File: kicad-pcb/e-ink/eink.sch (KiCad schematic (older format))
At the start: 80 parts, among them J2 Conn_01x39_Female, J3 Conn_01x08_Female, Q1 IRLML6402, U1 TS512BIYDT, U2 LT1945, U3 LM79L15ACM_NOPB, U4 LM78L15ACM_NOPB, U5 TPS62177DQC, U6 MCP23S17_SO, U8 MCP23S17_SO

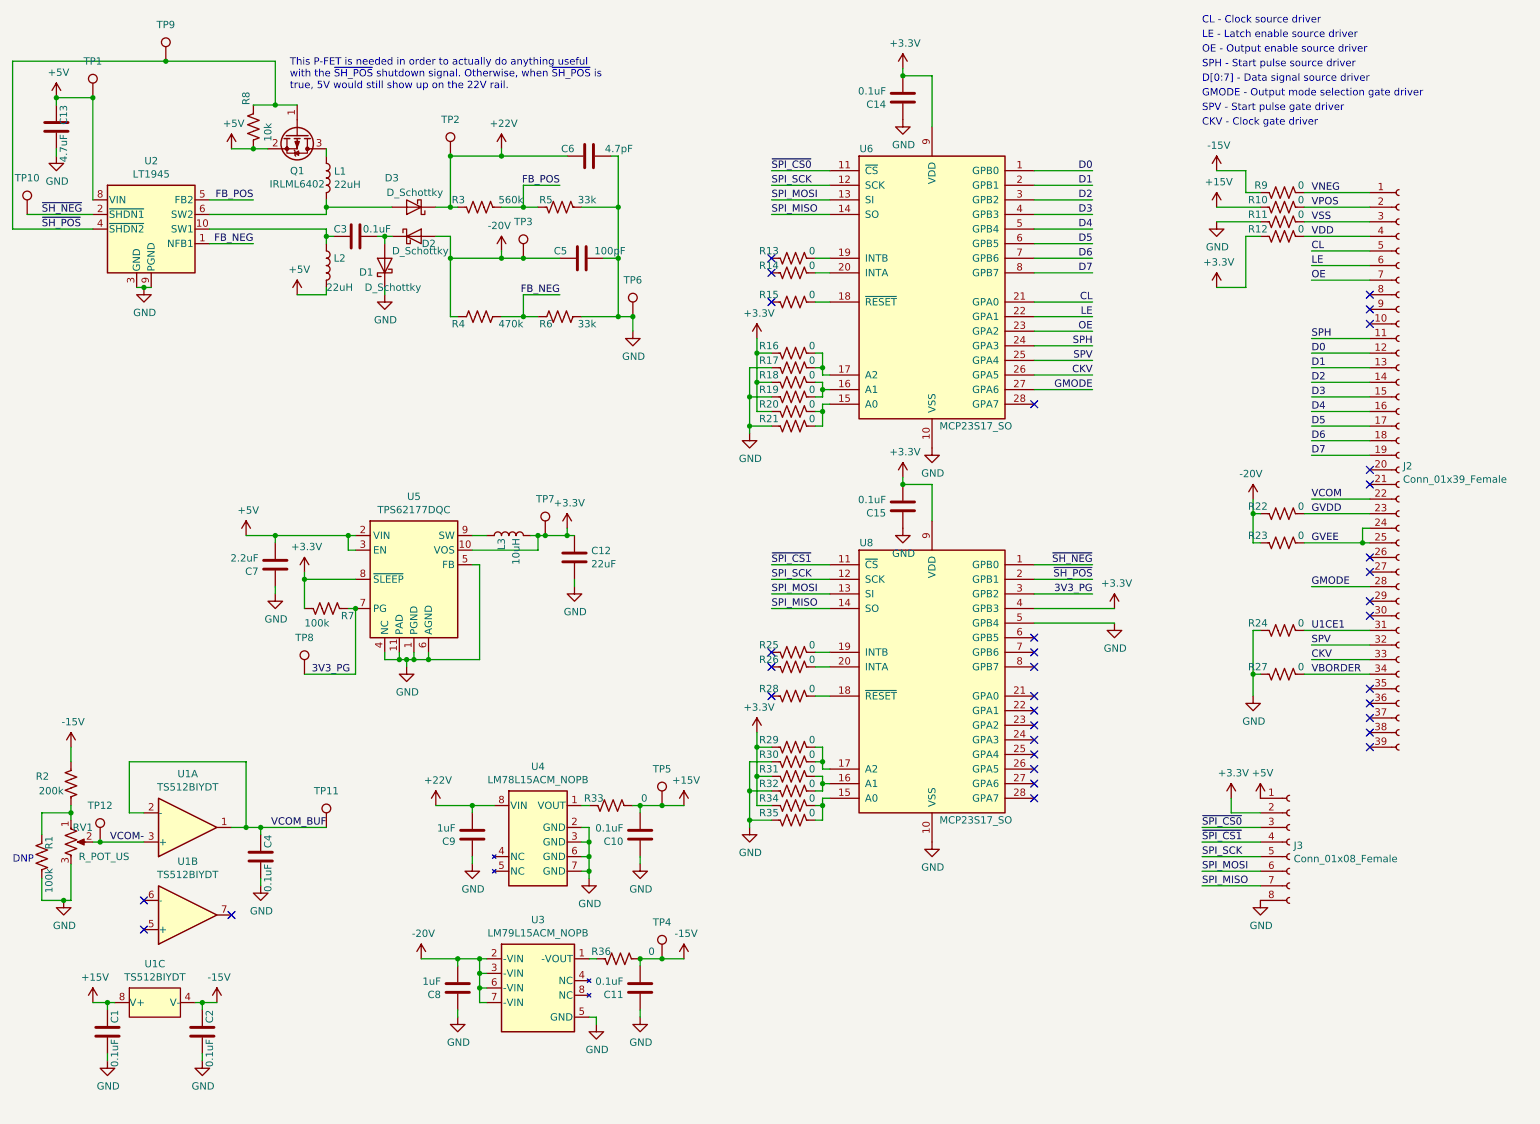
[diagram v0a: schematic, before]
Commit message: added additional SMPS control transistor circuit
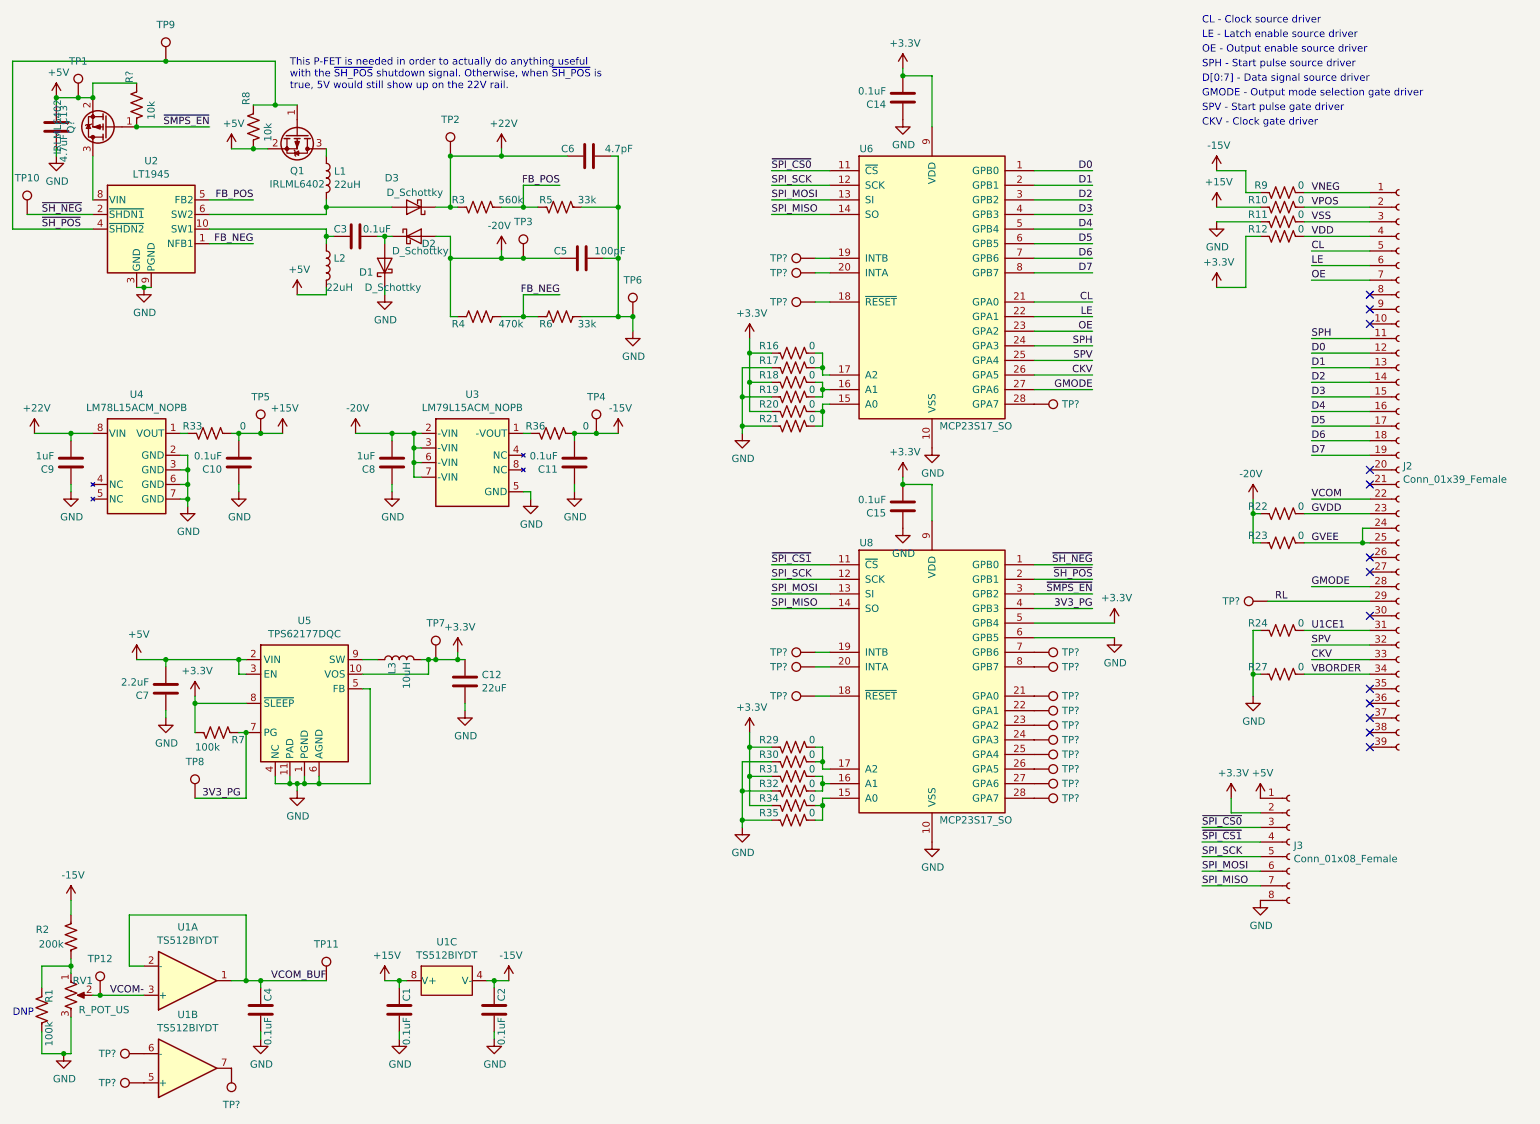
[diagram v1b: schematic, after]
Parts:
- removed R13, R14, R15, R25, R26, R28: 0, Resistor_SMD:R_0402_1005Metric, symbol Device:R_US
- added Q?: IRLML6402, Package_TO_SOT_SMD:SOT-23, symbol Transistor_FET:IRLML6402
- added R?: 10k, Resistor_SMD:R_0402_1005Metric, symbol Device:R_US
- added TP? (x21): TestPoint, symbol Connector:TestPoint
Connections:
- net +3V3: now also U8.5 (GPB4); no longer U8.4 (GPB3)
- net +5V: now also Q?.2 (S), R?.1; no longer U2.8 (VIN)
- net 3V3_PG: now also U8.4 (GPB3); no longer U8.3 (GPB2)
- net GND: now also U8.6 (GPB5); no longer U8.5 (GPB4)
- net at U1.5 (+): now also TP?.1
- net at U1.6 (-): now also TP?.1
- net at U1.7: now also TP?.1
- net RL: now reaches J2.29 (Pin_29)
- net RL: now also TP?.1
- net at U6.18 (~RESET~): now also TP?.1
- net at U6.19 (INTB): now also TP?.1
- net at U6.20 (INTA): now also TP?.1
- net at U6.28 (GPA7): now also TP?.1
- net at U8.18 (~RESET~): now also TP?.1
- net at U8.19 (INTB): now also TP?.1
- net at U8.20 (INTA): now also TP?.1
- net at U8.21 (GPA0): now also TP?.1
- net at U8.22 (GPA1): now also TP?.1
- net at U8.23 (GPA2): now also TP?.1
- net at U8.24 (GPA3): now also TP?.1
- net at U8.25 (GPA4): now also TP?.1
- net at U8.26 (GPA5): now also TP?.1
- net at U8.27 (GPA6): now also TP?.1
- net at U8.28 (GPA7): now also TP?.1
- net at U8.7 (GPB6): now also TP?.1
- net at U8.8 (GPB7): now also TP?.1
- new net: Q?.3 (D), U2.8 (VIN)
- new net ~SMPS_EN: Q?.1 (G), R?.2, U8.3 (GPB2)
- no-connect marks 35 -> 13
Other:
- moved on the sheet: C1, C10, C11, C12, C2, C4, C7, C8, C9, L3, R1, R2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

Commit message: added not about passive size
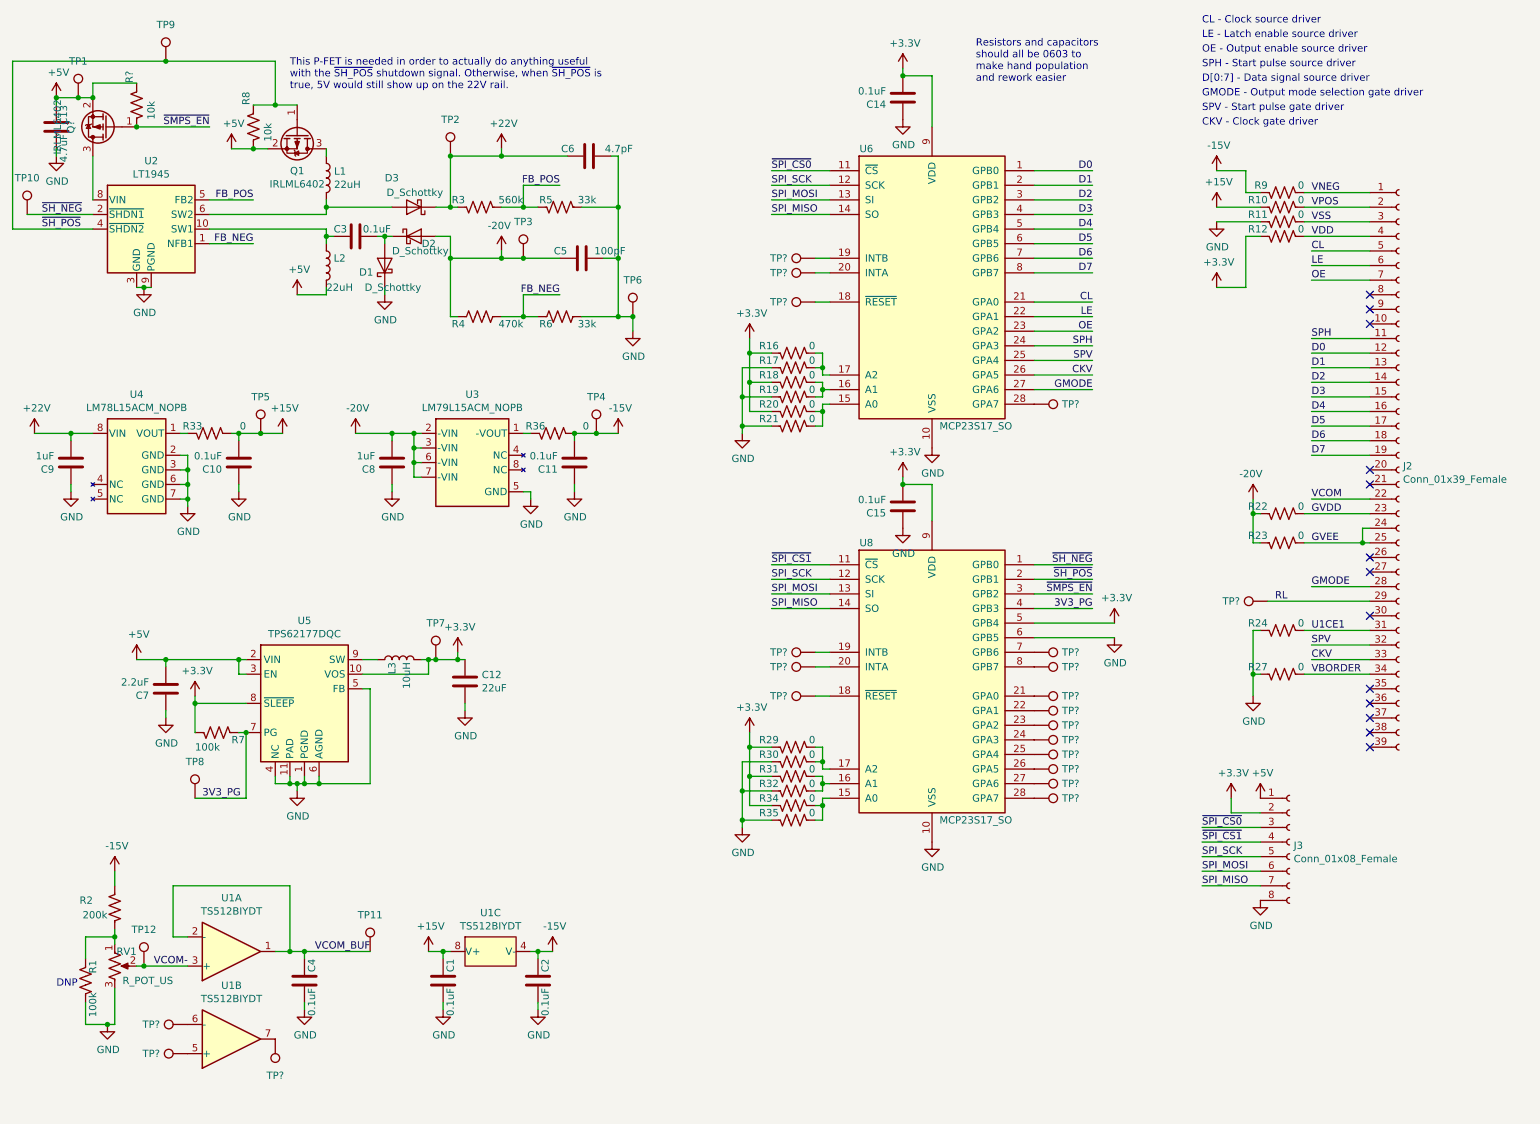
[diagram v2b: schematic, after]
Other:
- note added: "Resistors and capacitors\nshould all be 0603 to\nmake hand population\nand rework easier"
- moved on the sheet: C1, C2, C4, R1, R2, RV1, TP11, TP12, TP?, U1A, U1B, U1C
